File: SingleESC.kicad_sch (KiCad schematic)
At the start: 95 parts, among them J1 A, J2 B, J3 C, J4 BATT, J5 GND, J6 Conn_01x05, Q1 Q_NMOS_GDS, Q2 Q_NMOS_GDS, Q3 Q_NMOS_GDS, Q4 Q_NMOS_GDS, Q5 Q_NMOS_GDS, Q6 Q_NMOS_GDS, U1 HT7533-1_C14289, U2 AT32F421K8T7, U3 LMR51420YDDCR, U4 FD6288Q, U5 INA180A2

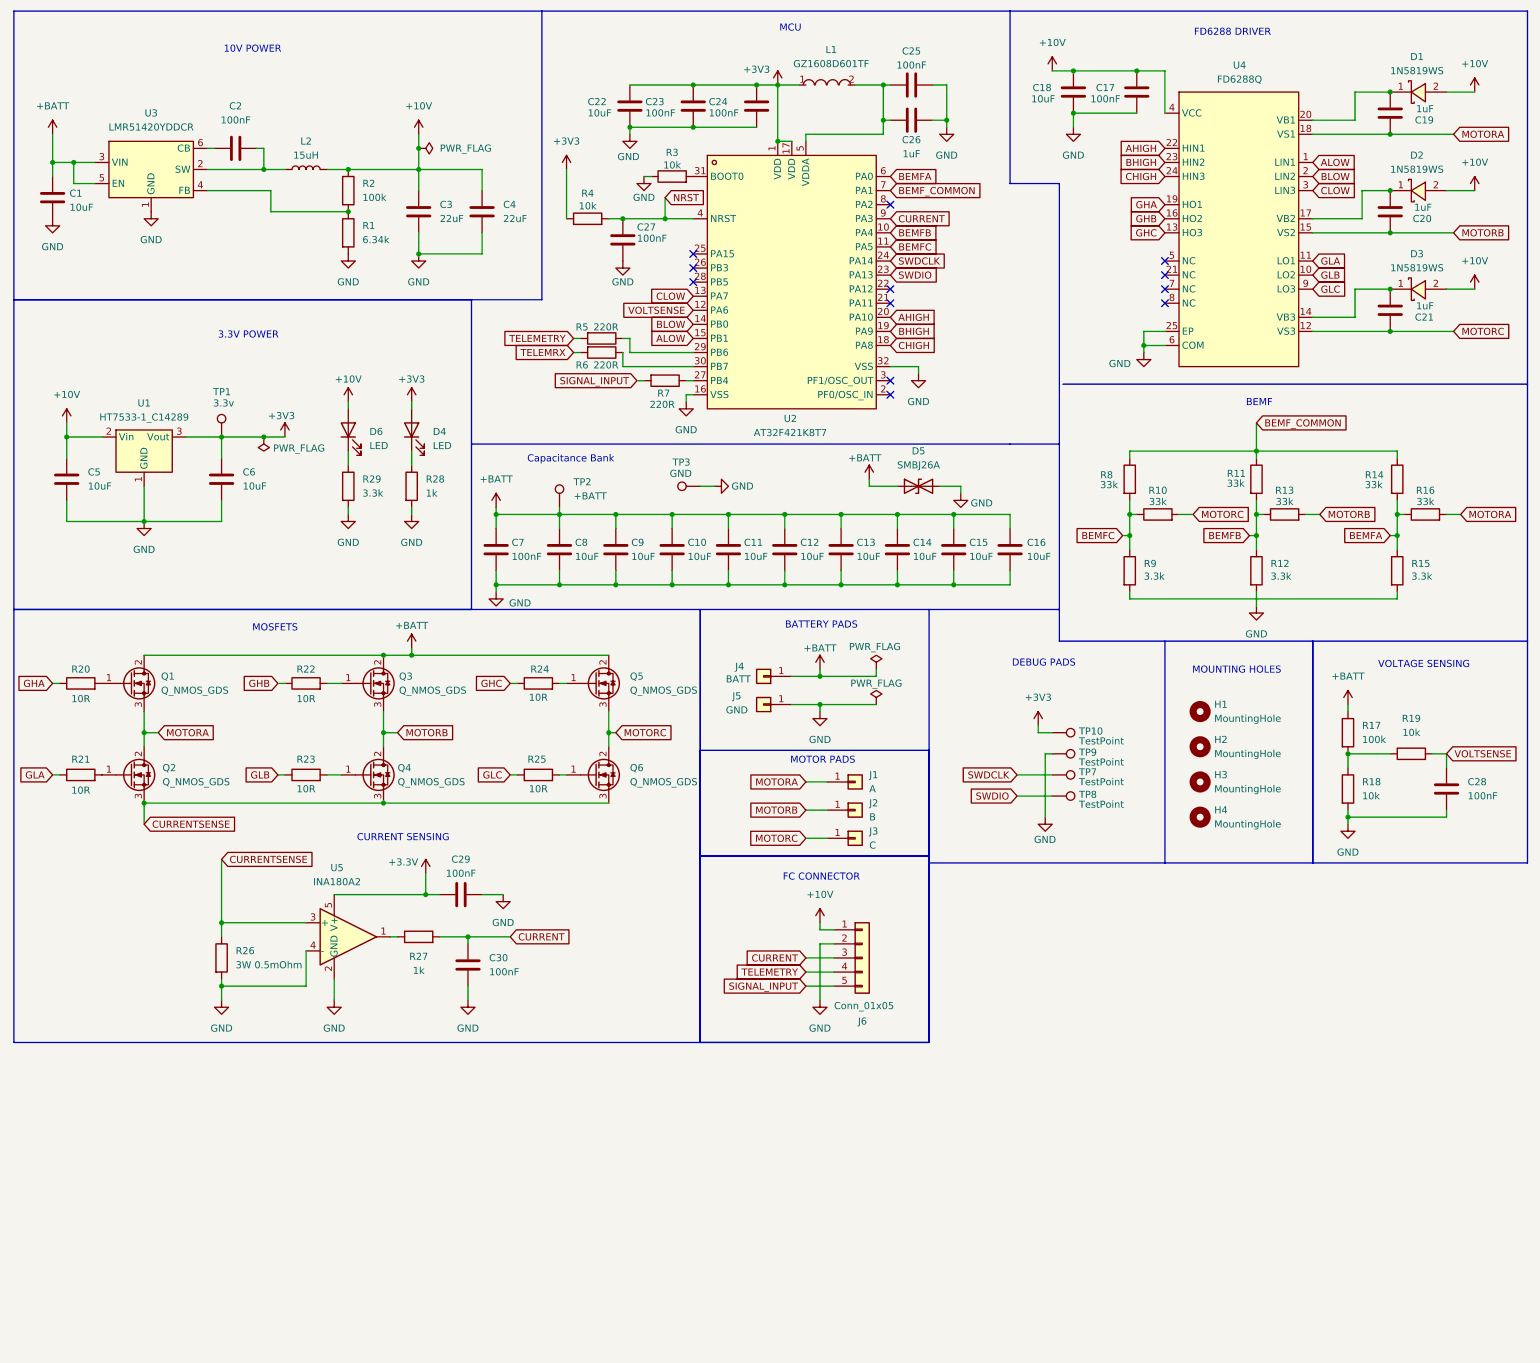
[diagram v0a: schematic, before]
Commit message: Add KiCad design review workflow and project files
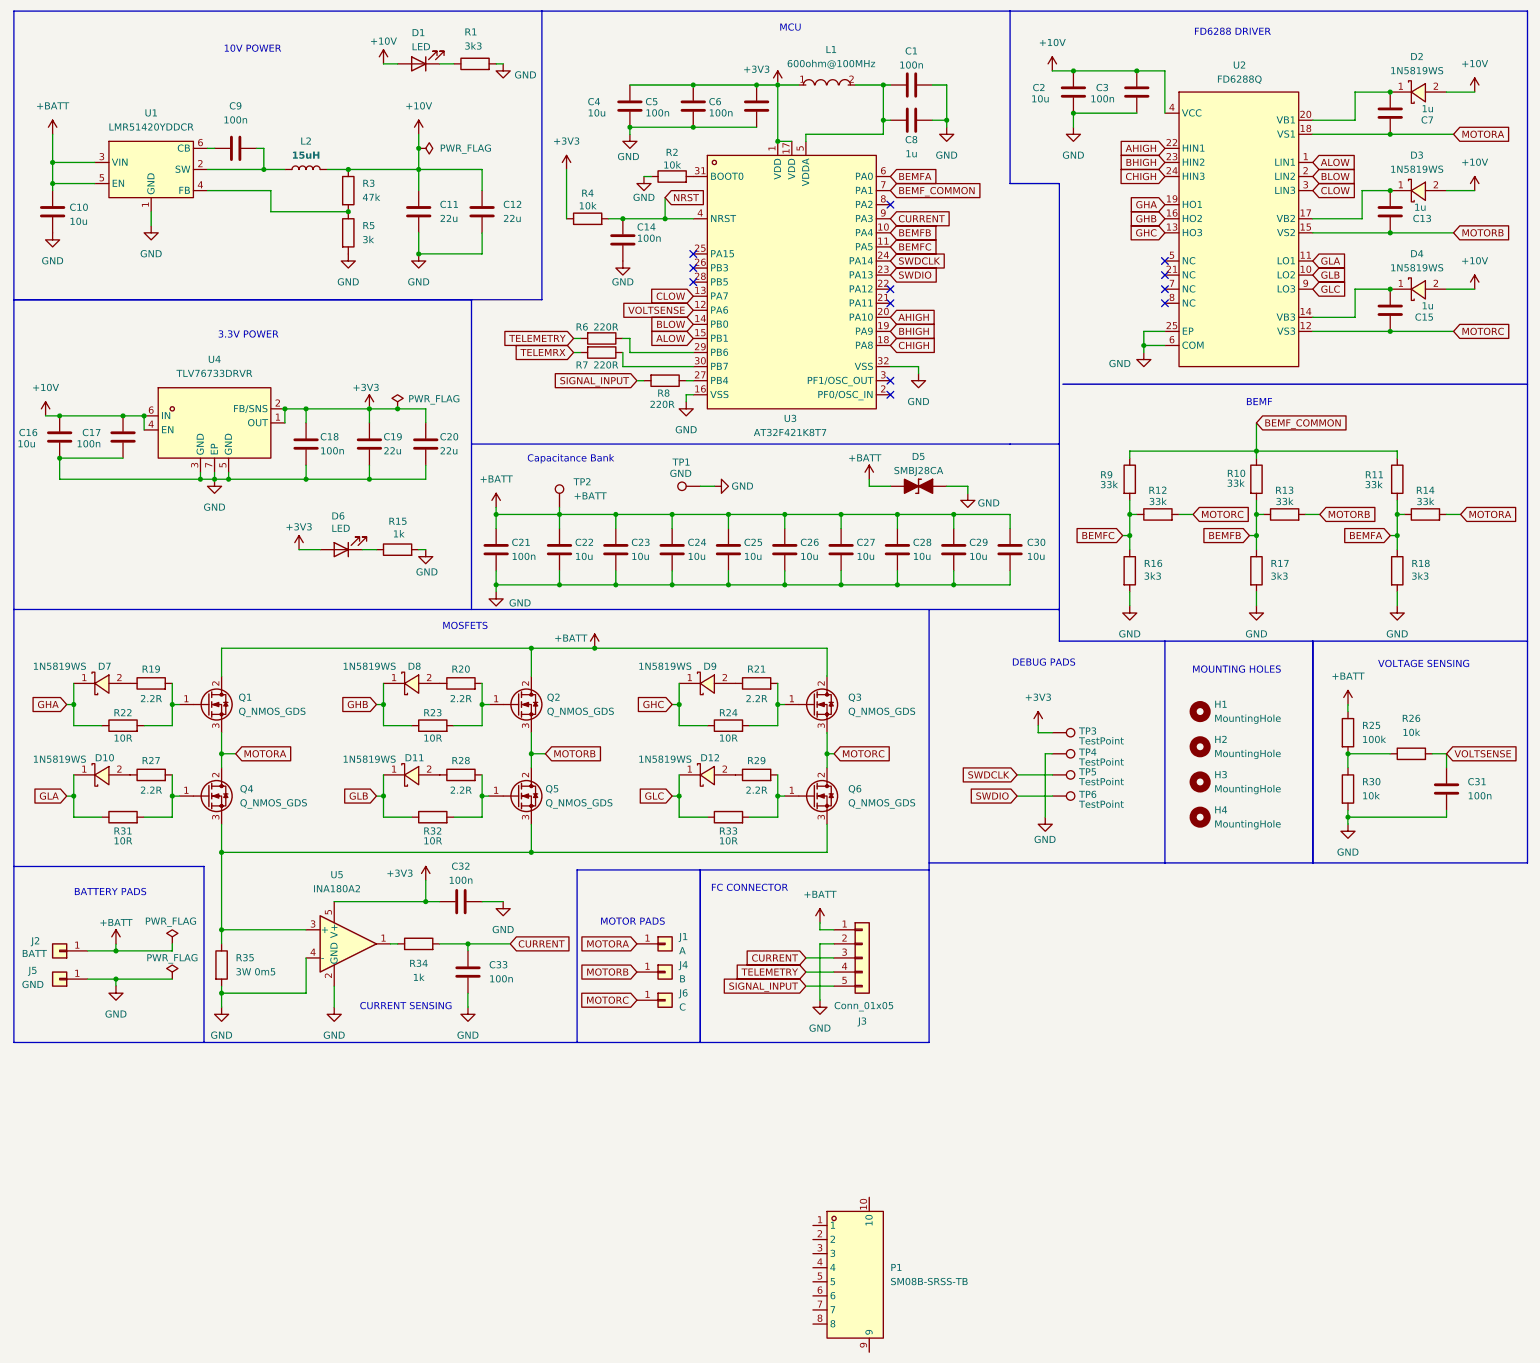
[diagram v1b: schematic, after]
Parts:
- removed C5, C6: 10uF, symbol Device:C
- removed D5: SMBJ26A, Diode_SMD:D_SMB, symbol Device:D_TVS
- removed R22, R25: 10R, symbol Device:R
- removed TP1: 3.3v, symbol Connector:TestPoint
- removed U1: HT7533-1_C14289, easyeda2kicad:SOT-89-3_L4.5-W2.5-P1.50-LS4.2-BR, symbol easyeda2kicad:HT7533-1_C14289
- added C16: 10u, symbol Device:C
- added C17, C18: 100n, symbol Device:C
- added C19, C20: 22u, symbol Device:C
- added D10, D11, D12, D7, D8, D9: 1N5819WS, easyeda2kicad:SOD-323_L1.8-W1.3-LS2.5-RD, symbol easyeda2kicad:1N5819WS
- added D5: SMBJ28CA, PCM_Diode_SMD_AKL:D_SMB_TVS, symbol PCM_Diode_TVS_AKL:SMBJ28CA
- added P1: SM08B-SRSS-TB, easyeda2kicad:CONN-TH_SM08B-SRSS-TB-LF-SN, symbol easyeda2kicad:SM08B-SRSS-TB
- added R19, R20, R27, R28, R29: 2.2R, symbol Device:R
- added R31, R32, R33: 10R, symbol Device:R
- added U4: TLV76733DRVR, easyeda2kicad:WSON-6_L2.0-W2.0-P0.65-TL-EP, symbol easyeda2kicad:TLV76733DRVR
- C1: renamed from C25; value 100nF -> 100n
- C10: renamed from C1; value 10uF -> 10u; LCSC (none) -> C13585
- C11: renamed from C3; value 22uF -> 22u; footprint (none) -> Capacitor_SMD:C_0805_2012Metric
- C12: renamed from C4; value 22uF -> 22u; footprint (none) -> Capacitor_SMD:C_0805_2012Metric
- C13: renamed from C20; value 1uF -> 1u
- C14: renamed from C27; value 100nF -> 100n
- C15: renamed from C21; value 1uF -> 1u
- C2: renamed from C18; value 10uF -> 10u
- C21: renamed from C7; value 100nF -> 100n
- C22: renamed from C8; value 10uF -> 10u
- C23: renamed from C9; value 10uF -> 10u
- C24: renamed from C10; value 10uF -> 10u
- C25: renamed from C11; value 10uF -> 10u
- C26: renamed from C12; value 10uF -> 10u
- C27: renamed from C13; value 10uF -> 10u
- C28: renamed from C14; value 10uF -> 10u
- C29: renamed from C15; value 10uF -> 10u
- C3: renamed from C17; value 100nF -> 100n
- C30: renamed from C16; value 10uF -> 10u
- C31: renamed from C28; value 100nF -> 100n
- C32: renamed from C29; value 100nF -> 100n
- C33: renamed from C30; value 100nF -> 100n
- C4: renamed from C22; value 10uF -> 10u
- C5: renamed from C23; value 100nF -> 100n
- C6: renamed from C24; value 100nF -> 100n
- C7: renamed from C19; value 1uF -> 1u
- C8: renamed from C26; value 1uF -> 1u
- C9: renamed from C2; value 100nF -> 100n; footprint (none) -> Capacitor_SMD:C_0402_1005Metric
- L1: value GZ1608D601TF -> 600ohm@100MHz
- L2: footprint Inductor_SMD:L_Sumida_CDMC6D28_7.25x6.5mm -> easyeda2kicad:IND-SMD_L7.1-W6.6
- Q1, Q6: footprint easyeda2kicad:DFN-8_L5.1-W5.7-P1.27-LS6.1-BL -> easyeda2kicad:POWERVDFN-8_L6.2-W5.2-P1.27-LS6.0-BL
- Q2: renamed from Q3; footprint easyeda2kicad:DFN-8_L5.1-W5.7-P1.27-LS6.1-BL -> easyeda2kicad:POWERVDFN-8_L6.2-W5.2-P1.27-LS6.0-BL
- Q3: renamed from Q5; footprint easyeda2kicad:DFN-8_L5.1-W5.7-P1.27-LS6.1-BL -> easyeda2kicad:POWERVDFN-8_L6.2-W5.2-P1.27-LS6.0-BL
- Q4: renamed from Q2; footprint easyeda2kicad:DFN-8_L5.1-W5.7-P1.27-LS6.1-BL -> easyeda2kicad:POWERVDFN-8_L6.2-W5.2-P1.27-LS6.0-BL
- Q5: renamed from Q4; footprint easyeda2kicad:DFN-8_L5.1-W5.7-P1.27-LS6.1-BL -> easyeda2kicad:POWERVDFN-8_L6.2-W5.2-P1.27-LS6.0-BL
- R1: renamed from R29; value 3.3k -> 3k3
- R16: renamed from R9; value 3.3k -> 3k3
- R17: renamed from R12; value 3.3k -> 3k3
- R18: renamed from R15; value 3.3k -> 3k3
- R2: renamed from R3; footprint (none) -> Resistor_SMD:R_0603_1608Metric
- R21: value 10R -> 2.2R
- R3: renamed from R2; value 100k -> 47k; footprint (none) -> Resistor_SMD:R_0402_1005Metric
- R35: renamed from R26; value 3W 0.5mOhm -> 3W 0m5
- R4: footprint (none) -> Resistor_SMD:R_0603_1608Metric
- R5: renamed from R1; value 6.34k -> 3k; footprint (none) -> Resistor_SMD:R_0603_1608Metric
- U2: renamed from U4; footprint easyeda2kicad:QFN-24_L4.0-W4.0-P0.50-BL-EP2.6 -> easyeda2kicad:WQFN-24_L4.0-W4.0-P0.50-TL-EP2.7; LCSC Part C328453 -> C54423134; MPN FD6288Q -> (none); Manufacturer Fortior Tech(峰岹) -> (none)
- renumbered D6 to D1, D1 to D2, D2 to D3, D3 to D4, D4 to D6, J4 to J2, J6 to J3, J2 to J4, J3 to J6, R11 to R10, R14 to R11, R10 to R12, R16 to R14, R28 to R15, R20 to R22, R17 to R25, R19 to R26, R18 to R30, R27 to R34, R5 to R6, R6 to R7, R7 to R8, R8 to R9, TP3 to TP1, TP10 to TP3, TP9 to TP4, TP7 to TP5, TP8 to TP6, U3 to U1, U2 to U3
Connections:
- net +3.3V is gone; now on net +3V3: C32.2, U5.5 (V+)
- net +10V: now also C16.1, C17.1, U4.4 (EN), U4.6 (IN); no longer J3.1 (Pin_1)
- net +3V3: now also C18.1, C19.1, C20.1, U4.1 (OUT), U4.2 (FB/SNS)
- net +BATT: now also J3.1 (Pin_1), D5.1 (K)
- net GHA: now also D7.1
- net GHB: now also R23.1, D8.1
- net GHC: now also D9.1
- net GLA: now also D10.1, R31.1; no longer R21.1
- net GLB: now also D11.1, R32.1; no longer R23.1
- net GLC: now also D12.1, R33.1
- net GND: now also R16.2, R18.2, C16.2, C17.2, C18.2, C19.2, C20.2, D5.2 (A), U4.3 (GND), U4.5 (GND), U4.7 (EP)
- net at Q6.1 (G): now also R29.2, R33.2
- net at Q5.1 (G): now also R28.2, R32.2; no longer R23.2
- net at Q2.1 (G): now also R23.2, R20.2
- net at Q4.1 (G): now also R27.2, R31.2; no longer R21.2
- net at Q1.1 (G), R22.2: now also R19.2
- net at Q3.1 (G), R24.2: now also R21.2
- net CURRENTSENSE: no longer names the net of Q4.3 (S), Q5.3 (S), Q6.3 (S), R35.1, U5.3 (+)
- new net: D10.2, R27.1
- new net: D7.2, R19.1
- new net: D11.2, R28.1
- new net: D12.2, R29.1
- new net: D8.2, R20.1
- new net: D9.2, R21.1
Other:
- moved on the sheet: C10, C32, C33, D1, D6, J1, J2, J4, J5, J6, Q1, Q2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

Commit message: Update schematic properties and generate new BOM mapped from old bom.md
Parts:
- C1, C14, C17, C18, C21, C3, C31, C32, C33, C5, C6: MPN (none) -> CC0603KRX7R9BB104; Manufacturer (none) -> YAGEO; lcsc (none) -> C14663
- C10, C16, C2, C22, C23, C24, C25, C26, C27, C28, C29, C30, C4: MPN (none) -> CL31A106KBHNNNE; Manufacturer (none) -> Samsung Electro-Mechanics; lcsc (none) -> C13585
- C11, C12, C19, C20: MPN (none) -> CL21A226MAQNNNE; Manufacturer (none) -> Samsung Electro-Mechanics; lcsc (none) -> C45783
- C13, C15, C7, C8: MPN (none) -> CL10A105KB8NNNC; Manufacturer (none) -> Samsung Electro-Mechanics; lcsc (none) -> C15849
- C9: MPN (none) -> CL05B104KO5NNNC; Manufacturer (none) -> Samsung Electro-Mechanics; lcsc (none) -> C1525
- D1, D6: MPN (none) -> KT-0603R; Manufacturer (none) -> Hubei KENTO Elec; lcsc (none) -> C2286
- D10, D11, D12, D2, D3, D4, D7, D8, D9: Manufacturer Hottech(合科泰) -> Guangdong Hottech; lcsc (none) -> C191023
- D5: MPN (none) -> SMBJ28CA; Manufacturer (none) -> R+O; lcsc (none) -> C19077583
- L1: Manufacturer Sunlord(顺络) -> Sunlord; lcsc (none) -> C1002
- L2: MPN (none) -> APH0630T150M; Manufacturer (none) -> APV; lcsc (none) -> C5349699
- P1: lcsc (none) -> C160407
- Q1, Q2, Q3, Q4, Q5, Q6: MPN (none) -> JMSH0401AGQ; Manufacturer (none) -> Jiangsu JieJie Microelectronics; lcsc (none) -> C7527437
- R1, R16, R17, R18: MPN (none) -> 0603WAF3301T5E; Manufacturer (none) -> UNI-ROYAL; lcsc (none) -> C22978
- R10, R11, R12, R13, R14, R9: MPN (none) -> 0603WAF3302T5E; Manufacturer (none) -> UNI-ROYAL; lcsc (none) -> C4216
- R15, R34: MPN (none) -> 0603WAF1001T5E; Manufacturer (none) -> UNI-ROYAL; lcsc (none) -> C21190
- R19, R20, R21, R27, R28, R29: MPN (none) -> 0603WAF220JT5E; Manufacturer (none) -> UNI-ROYAL; lcsc (none) -> C25877
- R2, R26, R30, R4: MPN (none) -> 0603WAF1002T5E; Manufacturer (none) -> UNI-ROYAL; lcsc (none) -> C25804
- R22, R23, R24, R31, R32, R33: MPN (none) -> 0603WAF100JT5E; Manufacturer (none) -> UNI-ROYAL; lcsc (none) -> C22859
- R25: MPN (none) -> 0603WAF1003T5E; Manufacturer (none) -> UNI-ROYAL; lcsc (none) -> C25803
- R3: MPN (none) -> 0402WGF4702TCE; Manufacturer (none) -> UNI-ROYAL; lcsc (none) -> C25792
- R35: MPN (none) -> HoCG251230m50F4S; Manufacturer (none) -> Milliohm; lcsc (none) -> C49067823
- R5: MPN (none) -> 0603WAF3001T5E; Manufacturer (none) -> UNI-ROYAL; lcsc (none) -> C4211
- R6, R7, R8: MPN (none) -> 0603WAF2200T5E; Manufacturer (none) -> UNI-ROYAL; lcsc (none) -> C22962
- U1: Manufacturer TI(德州仪器) -> TI; lcsc (none) -> C5383002
- U2: MPN (none) -> HXFD6288QFN24; Manufacturer (none) -> ZHHXDZ; lcsc (none) -> C54423134
- U3: Manufacturer ARTERY(雅特力) -> ARTERY; lcsc (none) -> C3029575
- U4: Manufacturer TI(德州仪器) -> TI; lcsc (none) -> C2848334
- U5: MPN (none) -> INA180A2IDBVR; Manufacturer (none) -> TI; lcsc (none) -> C192764
